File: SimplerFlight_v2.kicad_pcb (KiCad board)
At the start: 2 copper layers, 48 x 40 mm, 30 parts, among them J1 USB_B_Micro, J2 Conn_01x04_Pin, J3 Conn_01x04_Pin, J4 Conn_01x04_Pin, J5 Conn_01x04_Pin, SW1 SW_SPDT, U1 AMS1117-3.3, U2 STM32F401RETx, Y1 16MHz

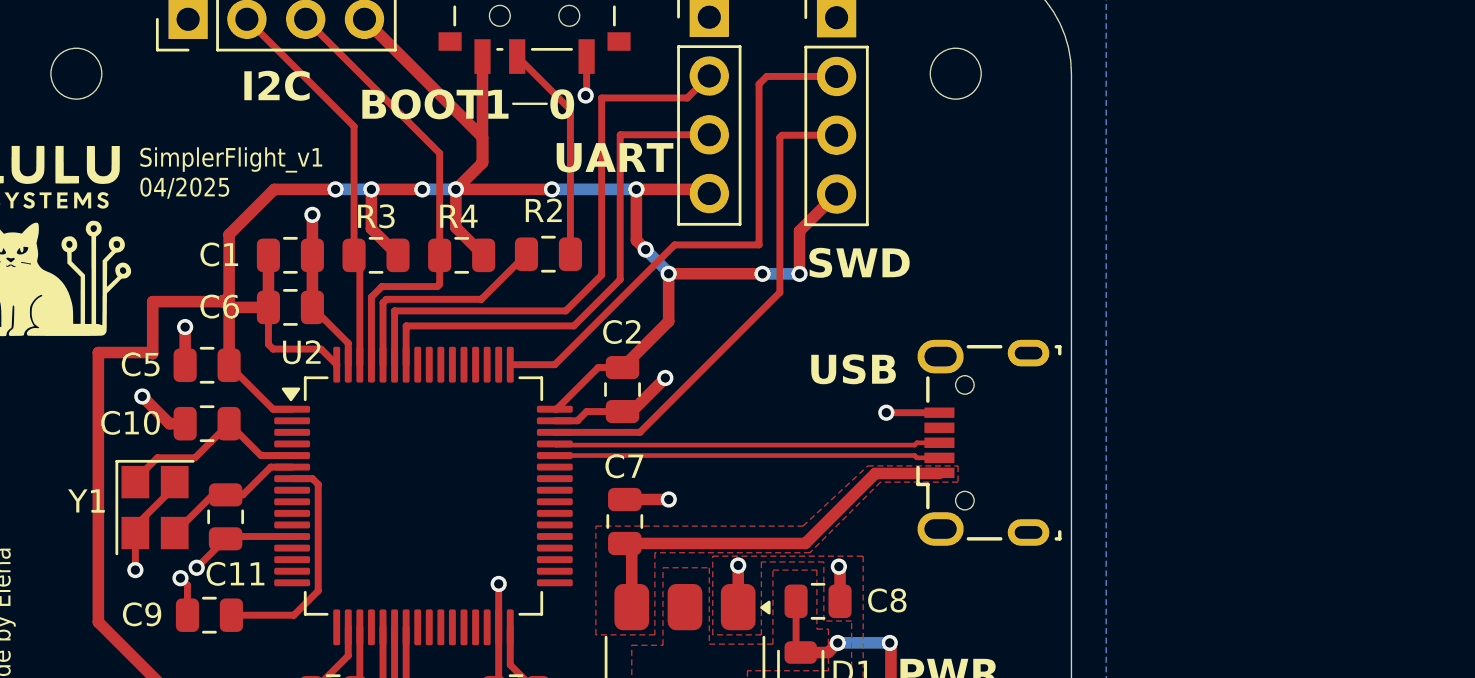
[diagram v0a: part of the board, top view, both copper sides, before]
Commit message: Add USB Mini B to replace USB Micro
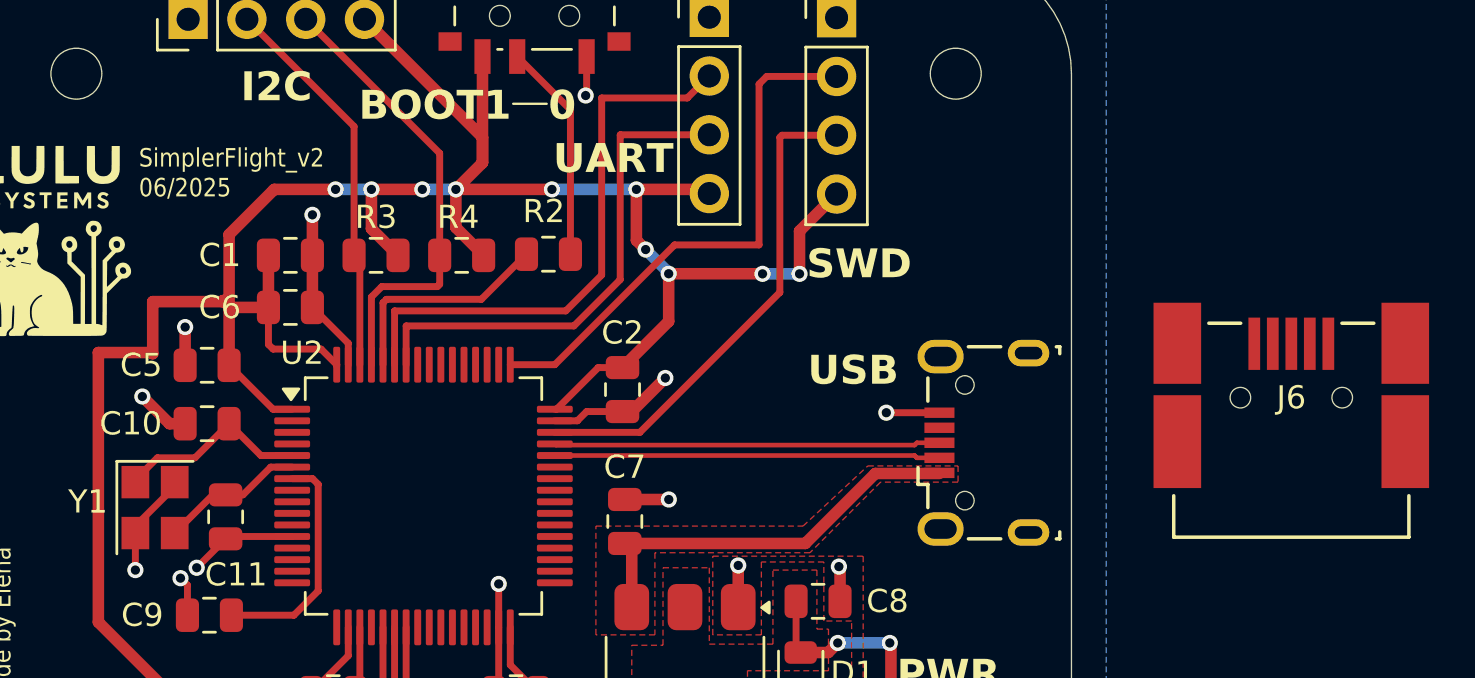
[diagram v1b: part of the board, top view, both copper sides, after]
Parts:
- added J6: 675031020, KiCADv6:CON00317_5_MOL, F.Cu at (153.5, 78.0)
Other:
- board text added: "SimplerFlight_v2 06/2025"
- board text removed: "SimplerFlight_v1 04/2025"

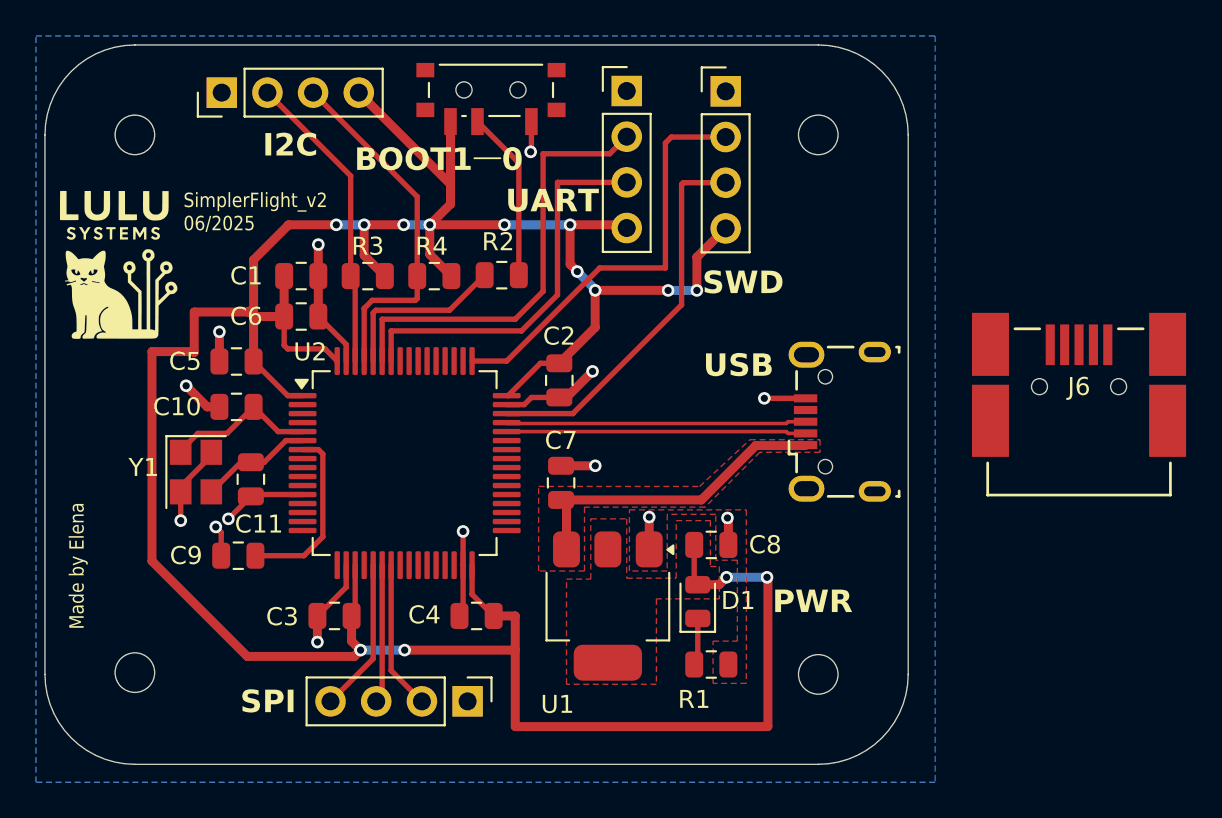
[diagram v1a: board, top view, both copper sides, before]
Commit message: Update readme and some silskreen labeles
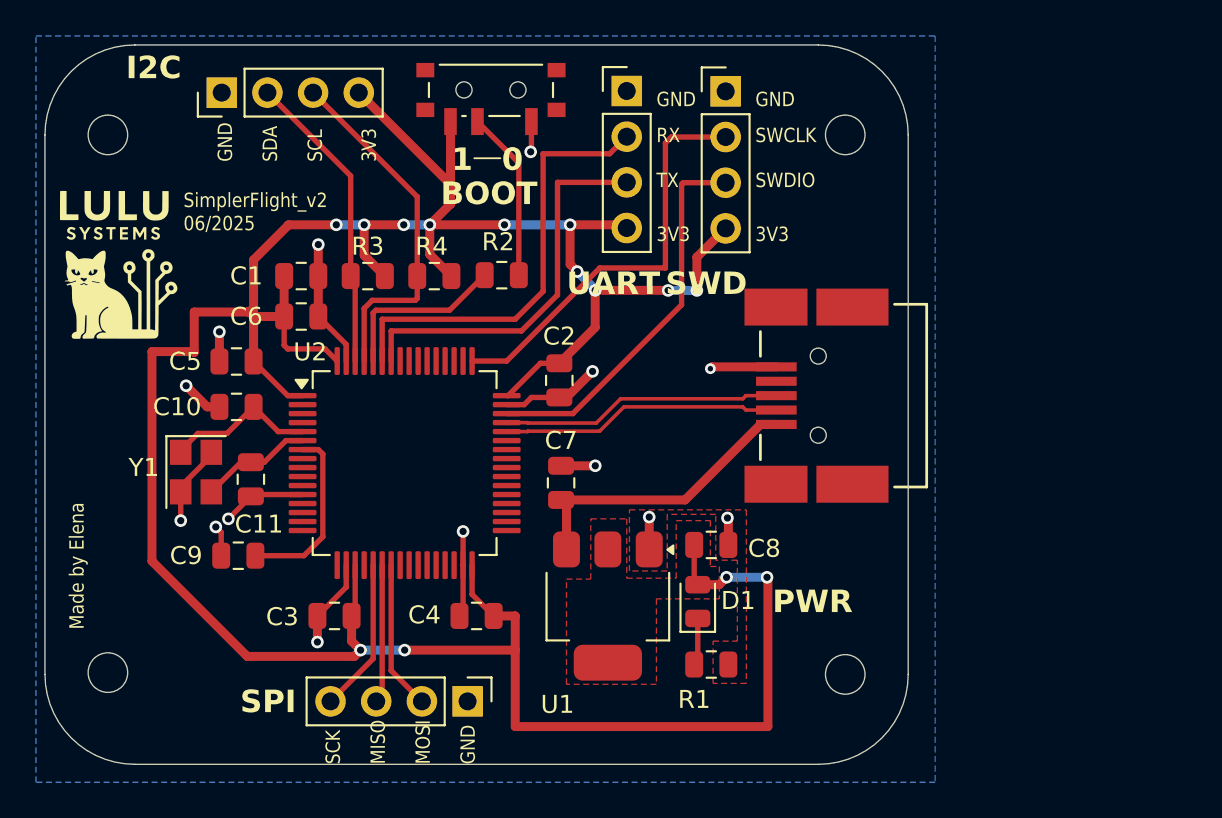
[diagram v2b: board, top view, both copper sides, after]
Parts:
- removed J1: USB_B_Micro, Connector_USB:USB_Micro-B_Wuerth_629105150521
- moved J6 14.5 mm to (139.0, 78.5), turned to 90 degrees
- moved H1 1.50 mm to (99.5, 64.0)
- moved H2 1.50 mm to (140.5, 64.0)
- moved H3 1.50 mm to (99.5, 93.9)
- moved H4 1.50 mm to (140.5, 94.0)
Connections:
- J6 pad 1: unconnected-(J6-Pad1) -> VBUS
- J6 pad 2: unconnected-(J6-Pad2) -> /USB_OTG_FS_D-
- J6 pad 3: unconnected-(J6-Pad3) -> /USB_OTG_FS_D+
- J6 pad 5: unconnected-(J6-Pad5) -> GND
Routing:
- net GND: track 46.5 -> 47.9 mm
- net VBUS: track 17.7 -> 16.6 mm
- net /USB_OTG_FS_D-: track 16.7 -> 15.6 mm
- net /USB_OTG_FS_D+: track 16.7 -> 15.7 mm
- removed copper zone on F.Cu, net VBUS
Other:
- board text added: "3V3"
- board text added: "GND"
- board text added: "MISO"
- board text added: "MOSI"
- board text added: "RX"
- board text added: "SCK"
- board text added: "SCL"
- board text added: "SDA"
- board text added: "SWCLK"
- board text added: "SWDIO"
- board text added: "TX"
- board text removed: "USB"

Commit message: Fix name
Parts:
- moved J5 0.50 mm to (119.5, 95.0)
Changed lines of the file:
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@@
 	(footprint "Connector_PinHeader_2.54mm:PinHeader_1x04_P2.54mm_Vertical"
 		(layer "F.Cu")
-		(at 119.5 95.5 -90)
+		(at 119.54 95 -90)
 		(descr "Through hole straight pin header, 1x04, 2.54mm pitch, single row")
 		(tags "Through hole pin header THT 1x04 2.54mm single row")

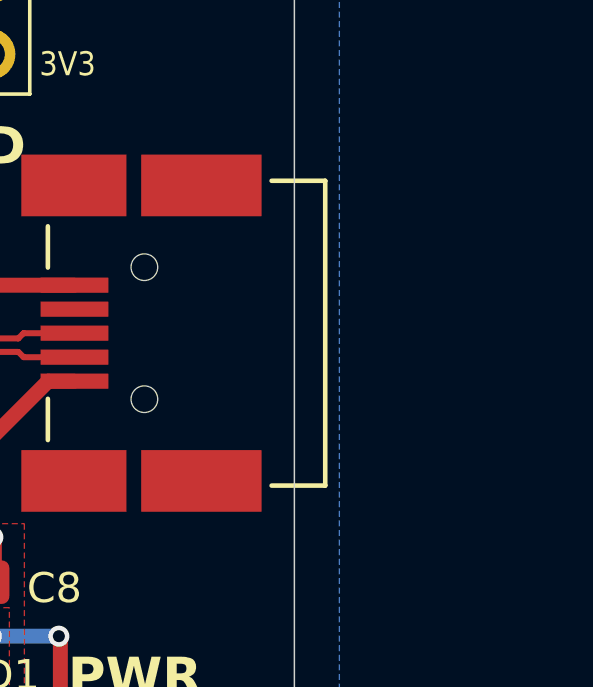
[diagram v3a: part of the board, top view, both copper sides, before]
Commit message: Reorganisation and draft of power supply
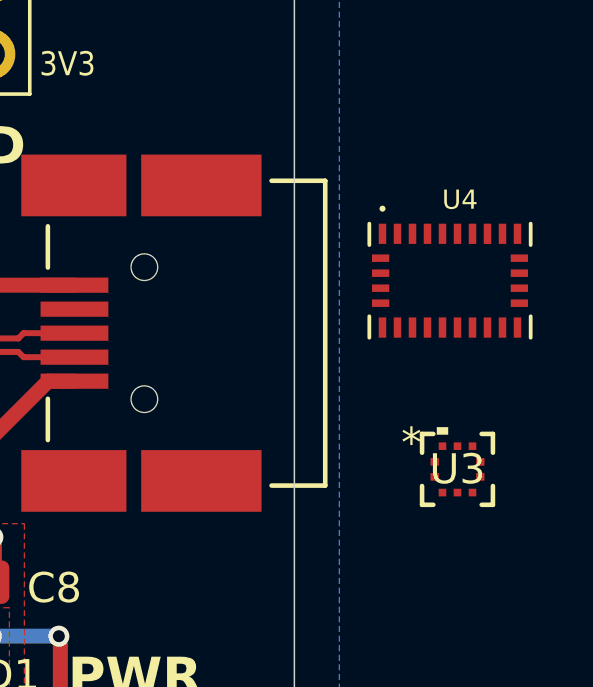
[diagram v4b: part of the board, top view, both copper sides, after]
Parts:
- added U3: BMP581, footprints:QFN10_BMP581_BOS, F.Cu at (149.4, 83.0)
- added U4: BNO085, BNO085:IC_BNO085, F.Cu at (149.2, 76.8)

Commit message: Initiliase main components
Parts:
- removed H1, H2, H3, H4: MountingHole, MountingHole:MountingHole_2.2mm_M2
- removed J2: Conn_01x04_Pin, Connector_PinHeader_2.54mm:PinHeader_1x04_P2.54mm_Vertical
- added BZ1: Buzzer, Buzzer_Beeper:Buzzer_CUI_CPT-9019S-SMT, F.Cu at (119.0, 64.5)
- added C12: C, Capacitor_SMD:C_0805_2012Metric, F.Cu at (153.1, 63.0)
- added C13: C, Capacitor_SMD:C_0805_2012Metric, F.Cu at (153.1, 66.0)
- added C14: C, Capacitor_SMD:C_0805_2012Metric, F.Cu at (157.5, 57.0)
- added C15: C, Capacitor_SMD:C_0805_2012Metric, F.Cu at (157.5, 60.0)
- added C16: C, Capacitor_SMD:C_0805_2012Metric, F.Cu at (157.5, 63.0)
- added C17: C, Capacitor_SMD:C_0805_2012Metric, F.Cu at (157.5, 66.0)
- added C18: C, Capacitor_SMD:C_0805_2012Metric, F.Cu at (161.9, 57.0)
- added C19: C, Capacitor_SMD:C_0805_2012Metric, F.Cu at (161.9, 60.0)
- added C20: C, Capacitor_SMD:C_0805_2012Metric, F.Cu at (180.6, 42.5)
- added C21: C, Capacitor_SMD:C_0805_2012Metric, F.Cu at (180.6, 45.5)
- added C22: C, Capacitor_SMD:C_0805_2012Metric, F.Cu at (180.6, 48.5)
- added C23: C, Capacitor_SMD:C_0805_2012Metric, F.Cu at (180.6, 51.5)
- added C24: C, Capacitor_SMD:C_0805_2012Metric, F.Cu at (180.6, 54.5)
- added C25: C, Capacitor_SMD:C_0805_2012Metric, F.Cu at (180.6, 57.5)
- added C26: C, Capacitor_SMD:C_0805_2012Metric, F.Cu at (180.6, 60.5)
- added D2: B540C-13-F, B540C_13_F:DIOM6959X245N, F.Cu at (95.5, 41.5)
- added D3: RED, LED_SMD:LED_0805_2012Metric, F.Cu at (171.6, 54.0)
- added D4: B540C-13-F, B540C_13_F:DIOM6959X245N, F.Cu at (95.5, 52.5)
- added D7: RED, LED_SMD:LED_0805_2012Metric, F.Cu at (171.6, 57.1)
- added D8: D, Diode_SMD:D_0805_2012Metric_Pad1.15x1.40mm_HandSolder, F.Cu at (162.0, 39.5)
- added F1: C1F-5, C1F_5:FUSC3215X83N, F.Cu at (102.0, 23.0)
- added F2: C1F-5, C1F_5:FUSC3215X83N, F.Cu at (102.0, 27.0)
- added J1: Battery 1, 39-28-1023:CONN_SD-5566-002_02_MOL, F.Cu at (83.6, 24.8)
- added J10: Cam 2, S05B_PASK_2_LF__SN_:CONN_S05B-PASK-2_JST, F.Cu at (84.1, 63.6)
- added J11: Cam 3, S05B_PASK_2_LF__SN_:CONN_S05B-PASK-2_JST, F.Cu at (100.6, 63.6)
- added J12: Encoder, Connector_PinHeader_1.00mm:PinHeader_1x04_P1.00mm_Vertical, F.Cu at (141.2, 62.0)
- added J13: Servo, Connector_PinHeader_1.00mm:PinHeader_1x03_P1.00mm_Vertical, F.Cu at (148.0, 63.0)
- added J14: DM3CS-SF, DM3CS_SF:HRS_DM3CS-SF, F.Cu at (179.5, 29.4)
- added J7: Battery 2, 39-28-1023:CONN_SD-5566-002_02_MOL, F.Cu at (94.1, 24.8)
- added J8: USB, KiCADv6:CON00317_5_MOL, F.Cu at (82.1, 51.1)
- added J9: Cam 1, S05B_PASK_2_LF__SN_:CONN_S05B-PASK-2_JST, F.Cu at (67.1, 63.6)
- added L1: L, Inductor_SMD:L_0805_2012Metric, F.Cu at (171.4, 42.2)
- added L2: L, Inductor_SMD:L_0805_2012Metric, F.Cu at (171.4, 45.0)
- added R10: R, Resistor_SMD:R_0805_2012Metric_Pad1.20x1.40mm_HandSolder, F.Cu at (166.9, 62.8)
- added R11: R, Resistor_SMD:R_0805_2012Metric_Pad1.20x1.40mm_HandSolder, F.Cu at (166.9, 65.7)
- added R12: 1k5, Resistor_SMD:R_0805_2012Metric_Pad1.20x1.40mm_HandSolder, F.Cu at (171.5, 63.0)
- added R13: R, Resistor_SMD:R_0805_2012Metric_Pad1.20x1.40mm_HandSolder, F.Cu at (185.2, 48.0)
- added R14: R, Resistor_SMD:R_0805_2012Metric_Pad1.20x1.40mm_HandSolder, F.Cu at (185.2, 50.9)
- added R15: R, Resistor_SMD:R_0805_2012Metric_Pad1.20x1.40mm_HandSolder, F.Cu at (185.2, 53.9)
- added R5: 1k5, Capacitor_SMD:C_0805_2012Metric, F.Cu at (161.9, 66.0)
- added R6: R, Resistor_SMD:R_0805_2012Metric_Pad1.20x1.40mm_HandSolder, F.Cu at (166.9, 51.0)
- added R7: R, Resistor_SMD:R_0805_2012Metric_Pad1.20x1.40mm_HandSolder, F.Cu at (166.9, 53.9)
- added R8: R, Resistor_SMD:R_0805_2012Metric_Pad1.20x1.40mm_HandSolder, F.Cu at (166.9, 56.9)
- added R9: R, Resistor_SMD:R_0805_2012Metric_Pad1.20x1.40mm_HandSolder, F.Cu at (166.9, 59.8)
- added SW2: System Reset, Button_Switch_SMD:SW_SPDT_PCM12, F.Cu at (115.3, 24.5)
- added U5: TPS62933, Package_TO_SOT_SMD:SOT-583-8, F.Cu at (143.8, 38.8)
- added U6: TPS62933, Package_TO_SOT_SMD:SOT-583-8, F.Cu at (153.5, 39.0)
- added U7: W25X40CLSNIG, W25X40CLSNIG:WIN_SN-8_WIN, F.Cu at (106.5, 37.0)
- added Y2: Crystal, Crystal:Crystal_SMD_0603-2Pin_6.0x3.5mm_HandSoldering, F.Cu at (157.5, 47.0)
- C7, C8: value 22uF -> ~
- D1: value RED -> BLUE
- J3: value Conn_01x04_Pin -> USART1 Header
- J4: value Conn_01x04_Pin -> I2C1 Header
- J5: value Conn_01x04_Pin -> SPI Header
- J6: value 675031020 -> SWD Header; footprint KiCADv6:CON00317_5_MOL -> Connector_PinHeader_2.54mm:PinHeader_1x05_P2.54mm_Vertical
- SW1: value SW_SPDT -> Boot Switch
- U3: footprint footprints:QFN10_BMP581_BOS -> BMP581:QFN10_BMP581_BOS
- moved J5 84.6 mm to (165.5, 23.9), turned to 0 degrees
- moved J4 62.8 mm to (156.0, 23.9), turned to 0 degrees
- moved D1 55.3 mm to (171.6, 51.0), turned to 0 degrees
- moved J6 54.6 mm to (136.0, 24.0), turned to 0 degrees
- moved R1 42.0 mm to (161.9, 63.0)
- moved J3 40.9 mm to (144.3, 23.9)
- moved C3 40.4 mm to (104.8, 51.0), turned to 0 degrees
- moved U3 40.4 mm to (166.0, 46.2)
- moved C4 39.7 mm to (104.8, 54.0), turned to 0 degrees
- moved Y1 39.1 mm to (119.0, 46.5), turned to 0 degrees
- moved C7 38.7 mm to (153.1, 57.0), turned to 0 degrees
- moved C11 38.7 mm to (113.7, 45.0), turned to 0 degrees
- moved U2 38.4 mm to (136.0, 49.5)
- moved SW1 37.8 mm to (127.3, 24.6), turned to 0 degrees
- moved C9 36.5 mm to (109.3, 51.0), turned to 0 degrees
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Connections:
- net /BOOT0 renamed /Microcontroller/BOOT0
- net /RCC_OSC_IN renamed /Microcontroller/RCC_OSC_IN
- net /RSS_OSC_OUT renamed /Microcontroller/RSS_OSC_OUT
- net /SPI1_MISO renamed SPI1_MISO
- net /SPI1_MOSI renamed SPI1_MOSI
- net /SPI1_SCK renamed SPI1_SCK
- net /SW_BOOT0 renamed /Microcontroller/SW_BOOT0
- net /USART1_RX renamed USART1_RX
- net /USART1_TX renamed USART1_TX
- C7 pad 1: VBUS -> Net-(D8-K)
- C9 pad 1: /NRST -> NRST
- D1 pad 1: /PWR_LED_K -> GND
- D1 pad 2: +3V3 -> Net-(D1-A)
- J4 pad 2: /12C1_SDA -> I2C1_SDA
- J4 pad 3: /12C1_SCL -> I2C1_SCL
- J6 pad 1: VBUS -> +3V3
- J6 pad 2: /USB_OTG_FS_D- -> /Microcontroller/SYS_JTMS-SWDIO
- J6 pad 3: /USB_OTG_FS_D+ -> /Microcontroller/SYS_JTCK-SWCLK
- J6 pad 4: unconnected-(J6-Pad4) -> NRST
- R1 pad 1: /PWR_LED_K -> +3V3
- R1 pad 2: GND -> Net-(D1-A)
- R3 pad 1: +3V3 -> I2C1_SDA
- R3 pad 2: /12C1_SDA -> +3V3
- R4 pad 1: +3V3 -> I2C1_SCL
- R4 pad 2: /12C1_SCL -> +3V3
- U1 pad 3: VBUS -> Net-(D8-K)
- U2 pad 44: /USB_OTG_FS_D- -> /Microcontroller/USB_OTG_FS_D-
- U2 pad 45: /USB_OTG_FS_D+ -> /Microcontroller/USB_OTG_FS_D+
- U2 pad 46: /SYS_JTMS-SWDIO -> /Microcontroller/SYS_JTMS-SWDIO
- U2 pad 49: /SYS_JTCK-SWCLK -> /Microcontroller/SYS_JTCK-SWCLK
- U2 pad 61: /12C1_SCL -> I2C1_SCL
- U2 pad 62: /12C1_SDA -> I2C1_SDA
- U2 pad 7: /NRST -> NRST
- U3 pad 1: unconnected-(U3-VDDIO-Pad1) -> +3V3
- U3 pad 10: unconnected-(U3-VDD-Pad10) -> +3V3
- U3 pad 2: unconnected-(U3-SCK-Pad2) -> SCK
- U3 pad 3: unconnected-(U3-VSS-Pad3) -> GND
- U3 pad 4: unconnected-(U3-SDI-Pad4) -> SDA
- U3 pad 5: unconnected-(U3-SDO-Pad5) -> GND
- U3 pad 6: unconnected-(U3-CSB-Pad6) -> +3V3
- U3 pad 7: unconnected-(U3-INT-Pad7) -> INT
- U3 pad 8: unconnected-(U3-VSS-Pad8) -> GND
- U3 pad 9: unconnected-(U3-VSS-Pad9) -> GND
- U4 pad 10: unconnected-(U4-CLKSEL0-Pad10) -> GND
- U4 pad 11: unconnected-(U4-~{RST}-Pad11) -> RST
- U4 pad 14: unconnected-(U4-~{H_INT}-Pad14) -> HINT
- U4 pad 15: unconnected-(U4-ENV_SCL-Pad15) -> Net-(U4-ENV_SCL)
- U4 pad 16: unconnected-(U4-ENV_SDA-Pad16) -> Net-(U4-ENV_SDA)
- U4 pad 17: unconnected-(U4-SA0/H_MOSI-Pad17) -> GND
- U4 pad 19: unconnected-(U4-H_SCL/SCK/RX-Pad19) -> SCL
- U4 pad 2: unconnected-(U4-GND-Pad2) -> GND
- U4 pad 20: unconnected-(U4-H_SDA/H_MISO/TX-Pad20) -> SDA
- U4 pad 25: unconnected-(U4-GNDIO-Pad25) -> GND
- U4 pad 26: unconnected-(U4-XOUT32/CLKSEL1-Pad26) -> Net-(U4-XOUT32/CLKSEL1)
- U4 pad 27: unconnected-(U4-XIN32-Pad27) -> Net-(U4-XIN32)
- U4 pad 28: unconnected-(U4-VDDIO-Pad28) -> +3V3
- U4 pad 3: unconnected-(U4-VDD-Pad3) -> +3V3
- U4 pad 4: unconnected-(U4-~{BOOT}-Pad4) -> Net-(U4-~{BOOT})
- U4 pad 5: unconnected-(U4-PS1-Pad5) -> GND
- U4 pad 6: unconnected-(U4-PS0/WAKE-Pad6) -> GND
- U4 pad 9: unconnected-(U4-CAP-Pad9) -> Net-(U4-CAP)
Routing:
- net +3V3: track 170.8 -> 0.00 mm, vias 14 -> 0
- net GND: track 47.9 -> 0.00 mm, vias 14 -> 0
- net USART1_RX: track 24.6 -> 0.00 mm
- net /SYS_JTCK-SWCLK: track 23.3 -> 0.00 mm
- net USART1_TX: track 21.9 -> 0.00 mm
- net /SYS_JTMS-SWDIO: track 21.4 -> 0.00 mm
- net /12C1_SCL: track 20.0 -> 0.00 mm
- net /12C1_SDA: track 16.9 -> 0.00 mm
- net VBUS: track 16.6 -> 0.00 mm
- net /USB_OTG_FS_D+: track 15.7 -> 0.00 mm
- net /USB_OTG_FS_D-: track 15.6 -> 0.00 mm
- net /NRST: track 10.0 -> 0.00 mm
- net /Microcontroller/BOOT0: track 9.74 -> 0.00 mm
- net /Microcontroller/SW_BOOT0: track 9.49 -> 0.00 mm
- net SPI1_SCK: track 8.56 -> 0.00 mm
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- removed copper zone on F.Cu, net +3V3
- removed copper zone on B.Cu, net GND
- removed copper zone on F.Cu, net GND
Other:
- board outline removed
- board text added: "CAS 2025 07/2025"
- board text removed: "0"
- board text removed: "1"
- board text removed: "3V3"
- board text removed: "BOOT"
- board text removed: "GND"
- board text removed: "I2C"
- board text removed: "MISO"
- board text removed: "MOSI"
- board text removed: "Made by Elena"
- board text removed: "PWR"
- board text removed: "RX"
- board text removed: "SCK"
- board text removed: "SCL"
- board text removed: "SDA"
- board text removed: "SPI"
- board text removed: "SWCLK"
- board text removed: "SWD"
- board text removed: "SWDIO"
- board text removed: "SimplerFlight_v2 06/2025"
- board text removed: "TX"
- board text removed: "UART"
